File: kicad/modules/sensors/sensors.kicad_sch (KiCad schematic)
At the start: 44 parts, among them J1 Bus_PCI_Express_x1, J2 TYPE-C-31-M-04, J3 Conn_01x02, U2 RP2040, U4 W25Q128JVP, U5 BMP388, U8 BNO055, U9 MCP25625T-E/ML, X1 ABM8-272-T3, Y1 ABS07-32.768KHZ-T, Y2 X322516MLB4SI

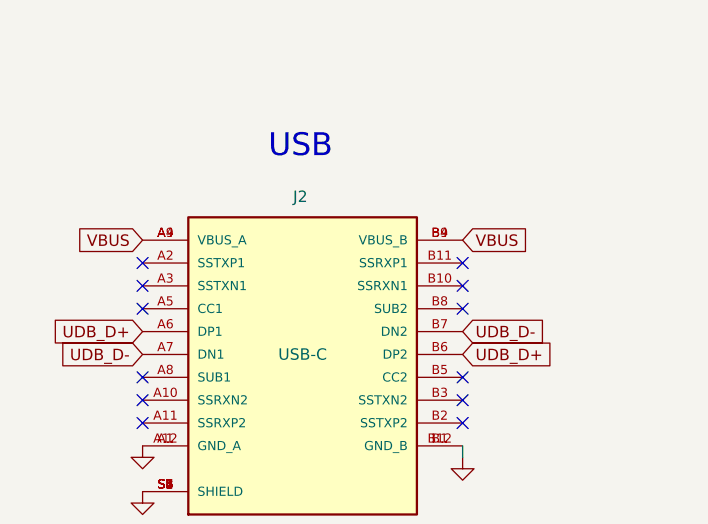
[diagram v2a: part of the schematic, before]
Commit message: add no connect to USB power pins
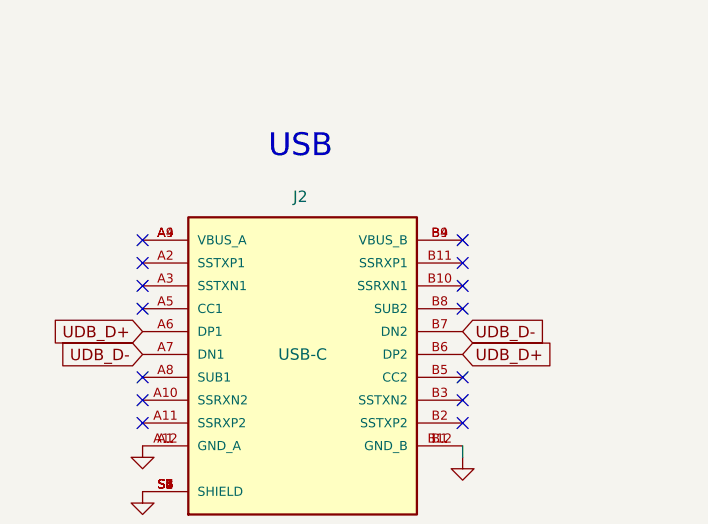
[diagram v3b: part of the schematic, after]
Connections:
- net VBUS: no longer names the net of J2.A4 (VBUS_A), J2.A9 (VBUS_A)
- net VBUS: no longer J2.B4 (VBUS_B), J2.B9 (VBUS_B)
- new net: J2.B4 (VBUS_B), J2.B9 (VBUS_B)
- no-connect marks 18 -> 20
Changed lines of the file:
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@@
+	)
+	(no_connect
+		(at 93.98 62.23)
+	)
+	(no_connect
+		(at 58.42 67.31)
+	)
+	(no_connect
+		(at 58.42 80.01)
+	)
+	(no_connect
+		(at 346.71 342.9)
+	)
+	(no_connect
+		(at 346.71 345.44)
 	)
 	(no_connect
@@
 	)
 	(no_connect
-		(at 58.42 67.31)
-	)
-	(no_connect
-		(at 58.42 80.01)
-	)
-	(no_connect
-		(at 346.71 342.9)
-	)
-	(no_connect
-		(at 346.71 345.44)
-	)
-	(no_connect
 		(at 93.98 77.47)
 	)
@@
 	(no_connect
 		(at 93.98 82.55)
+	)
+	(no_connect
+		(at 58.42 62.23)
 	)
 	(no_connect
@@
 		)
 	)
-	(global_label "VBUS"
-		(shape input)
-		(at 58.42 62.23 180)
+	(global_label "SI"
+		(shape input)
+		(at 378.46 220.98 0)
+		(fields_autoplaced yes)
+		(effects
+			(font
+				(size 1.27 1.27)
+			)
+			(justify left)
+		)
+		(property "Intersheetrefs" "${INTERSHEET_REFS}"
+			(at 383.2595 220.98 0)
+			(effects
+				(font
+					(size 1.27 1.27)
+				)
+				(justify left)
+				(hide yes)
+			)
+		)
+	)
+	(global_label "SO"
+		(shape input)
+		(at 378.46 223.52 0)
+		(fields_autoplaced yes)
+		(effects
+			(font
+				(size 1.27 1.27)
+			)
+			(justify left)
+		)
+		(property "Intersheetrefs" "${INTERSHEET_REFS}"
+			(at 383.9852 223.52 0)
+			(effects
+				(font
+					(size 1.27 1.27)
+				)
+				(justify left)
+				(hide yes)
+			)
+		)
+	)
+	(global_label "BMPINT"
+		(shape input)
+		(at 378.46 200.66 0)
+		(fields_autoplaced yes)
+		(effects
+			(font
+				(size 1.27 1.27)
+			)
+			(justify left)
+		)
+		(property "Intersheetrefs" "${INTERSHEET_REFS}"
+			(at 388.3395 200.66 0)
+			(effects
+				(font
+					(size 1.27 1.27)
+				)
+				(justify left)
+				(hide yes)
+			)
+		)
+	)
+	(global_label "tx"
+		(shape input)
+		(at 397.51 363.22 0)
+		(fields_autoplaced yes)
+		(effects
+			(font
+				(size 1.27 1.27)
+			)
+			(justify left)
+		)
+		(property "Intersheetrefs" "${INTERSHEET_REFS}"
+			(at 402.249 363.22 0)
+			(effects
+				(font
+					(size 1.27 1.27)
+				)
+				(justify left)
+				(hide yes)
+			)
+		)
+	)
+	(global_label "CS"
+		(shape input)
+		(at 346.71 330.2 180)
 		(fields_autoplaced yes)
 		(effects
@@
 		)
 		(property "Intersheetrefs" "${INTERSHEET_REFS}"
-			(at 50.5362 62.23 0)
+			(at 341.2453 330.2 0)
 			(effects
 				(font
@@
 		)
 	)
+	(global_label "BOOT_LOAD"
+		(shape input)
+		(at 471.17 278.13 180)
+		(fields_autoplaced yes)
+		(effects
+			(font
+				(size 1.27 1.27)
+			)
+			(justify right)
+		)
+		(property "Intersheetrefs" "${INTERSHEET_REFS}"
+			(at 457.6014 278.13 0)
+			(effects
+				(font
+					(size 1.27 1.27)
+				)
+				(justify right)
+				(hide yes)
+			)
+		)
+	)
 	(global_label "SI"
 		(shape input)
-		(at 378.46 220.98 0)
+		(at 397.51 335.28 0)
 		(fields_autoplaced yes)
 		(effects
@@
 		)
 		(property "Intersheetrefs" "${INTERSHEET_REFS}"
-			(at 383.2595 220.98 0)
+			(at 402.3095 335.28 0)
 			(effects
 				(font
@@
 		)
 	)
-	(global_label "SO"
-		(shape input)
-		(at 378.46 223.52 0)
+	(global_label "SCL"
+		(shape input)
+		(at 491.49 288.29 180)
+		(fields_autoplaced yes)
+		(effects
+			(font
+				(size 1.27 1.27)
+			)
+			(justify right)
+		)
+		(property "Intersheetrefs" "${INTERSHEET_REFS}"
+			(at 484.9972 288.29 0)
+			(effects
+				(font
+					(size 1.27 1.27)
+				)
+				(justify right)
+				(hide yes)
+			)
+		)
+	)
+	(global_label "CANSTBY"
+		(shape input)
+		(at 378.46 233.68 0)
 		(fields_autoplaced yes)
 		(effects
@@
 		)
 		(property "Intersheetrefs" "${INTERSHEET_REFS}"
-			(at 383.9852 223.52 0)
+			(at 389.67 233.68 0)
 			(effects
 				(font
@@
 		)
 	)
-	(global_label "BMPINT"
-		(shape input)
-		(at 378.46 200.66 0)
+	(global_label "OSC2"
+		(shape input)
+		(at 397.51 353.06 0)
 		(fields_autoplaced yes)
 		(effects
@@
 		)
 		(property "Intersheetrefs" "${INTERSHEET_REFS}"
-			(at 388.3395 200.66 0)
-			(effects
-				(font
-					(size 1.27 1.27)
-				)
-				(justify left)
-				(hide yes)
-			)
-		)
-	)
-	(global_label "tx"
-		(shape input)
-		(at 397.51 363.22 0)
-		(fields_autoplaced yes)
-		(effects
-			(font
-				(size 1.27 1.27)
-			)
-			(justify left)
-		)
-		(property "Intersheetrefs" "${INTERSHEET_REFS}"
-			(at 402.249 363.22 0)
-			(effects
-				(font
-					(size 1.27 1.27)
-				)
-				(justify left)
-				(hide yes)
-			)
-		)
-	)
-	(global_label "CS"
-		(shape input)
-		(at 346.71 330.2 180)
-		(fields_autoplaced yes)
-		(effects
-			(font
-				(size 1.27 1.27)
-			)
-			(justify right)
-		)
-		(property "Intersheetrefs" "${INTERSHEET_REFS}"
-			(at 341.2453 330.2 0)
-			(effects
-				(font
-					(size 1.27 1.27)
-				)
-				(justify right)
-				(hide yes)
-			)
-		)
-	)
-	(global_label "BOOT_LOAD"
-		(shape input)
-		(at 471.17 278.13 180)
-		(fields_autoplaced yes)
-		(effects
-			(font
-				(size 1.27 1.27)
-			)
-			(justify right)
-		)
-		(property "Intersheetrefs" "${INTERSHEET_REFS}"
-			(at 457.6014 278.13 0)
-			(effects
-				(font
-					(size 1.27 1.27)
-				)
-				(justify right)
-				(hide yes)
-			)
-		)
-	)
-	(global_label "SI"
-		(shape input)
-		(at 397.51 335.28 0)
-		(fields_autoplaced yes)
-		(effects
-			(font
-				(size 1.27 1.27)
-			)
-			(justify left)
-		)
-		(property "Intersheetrefs" "${INTERSHEET_REFS}"
-			(at 402.3095 335.28 0)
-			(effects
-				(font
-					(size 1.27 1.27)
-				)
-				(justify left)
-				(hide yes)
-			)
-		)
-	)
-	(global_label "SCL"
-		(shape input)
-		(at 491.49 288.29 180)
-		(fields_autoplaced yes)
-		(effects
-			(font
-				(size 1.27 1.27)
-			)
-			(justify right)
-		)
-		(property "Intersheetrefs" "${INTERSHEET_REFS}"
-			(at 484.9972 288.29 0)
-			(effects
-				(font
-					(size 1.27 1.27)
-				)
-				(justify right)
-				(hide yes)
-			)
-		)
-	)
-	(global_label "CANSTBY"
-		(shape input)
-		(at 378.46 233.68 0)
-		(fields_autoplaced yes)
-		(effects
-			(font
-				(size 1.27 1.27)
-			)
-			(justify left)
-		)
-		(property "Intersheetrefs" "${INTERSHEET_REFS}"
-			(at 389.67 233.68 0)
-			(effects
-				(font
-					(size 1.27 1.27)
-				)
-				(justify left)
-				(hide yes)
-			)
-		)
-	)
-	(global_label "OSC2"
-		(shape input)
-		(at 397.51 353.06 0)
-		(fields_autoplaced yes)
-		(effects
-			(font
-				(size 1.27 1.27)
-			)
-			(justify left)
-		)
-		(property "Intersheetrefs" "${INTERSHEET_REFS}"
 			(at 405.5147 353.06 0)
 			(effects
 				(font
-					(size 1.27 1.27)
-				)
-				(justify left)
-				(hide yes)
-			)
-		)
-	)
-	(global_label "VBUS"
-		(shape input)
-		(at 93.98 62.23 0)
-		(fields_autoplaced yes)
-		(effects
-			(font
-				(size 1.27 1.27)
-			)
-			(justify left)
-		)
-		(property "Intersheetrefs" "${INTERSHEET_REFS}"
-			(at 101.8638 62.23 0)
-			(effects
-				(font

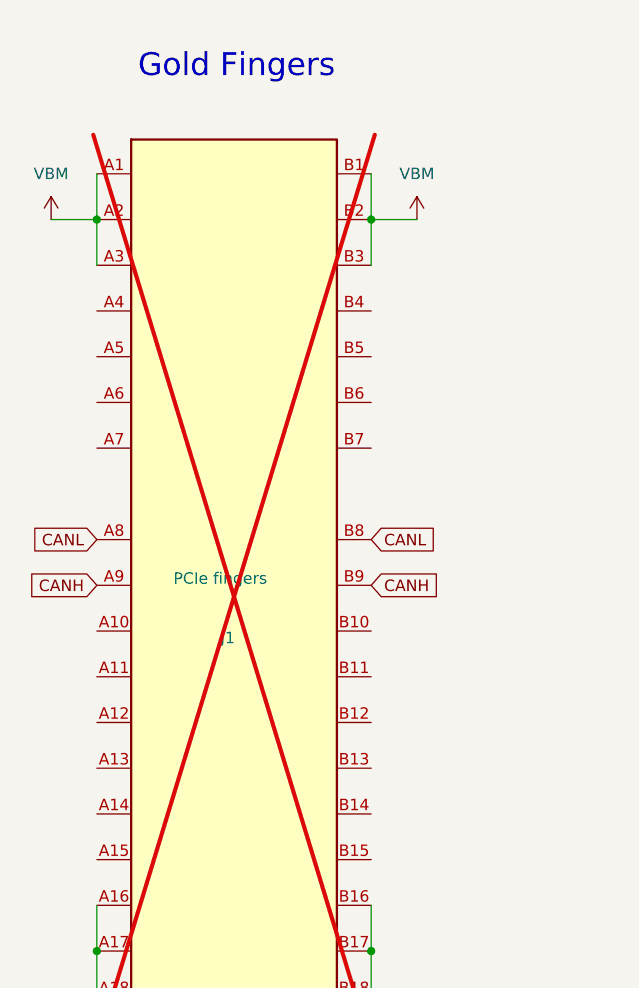
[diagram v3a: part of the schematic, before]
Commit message: reassign PCIe pins
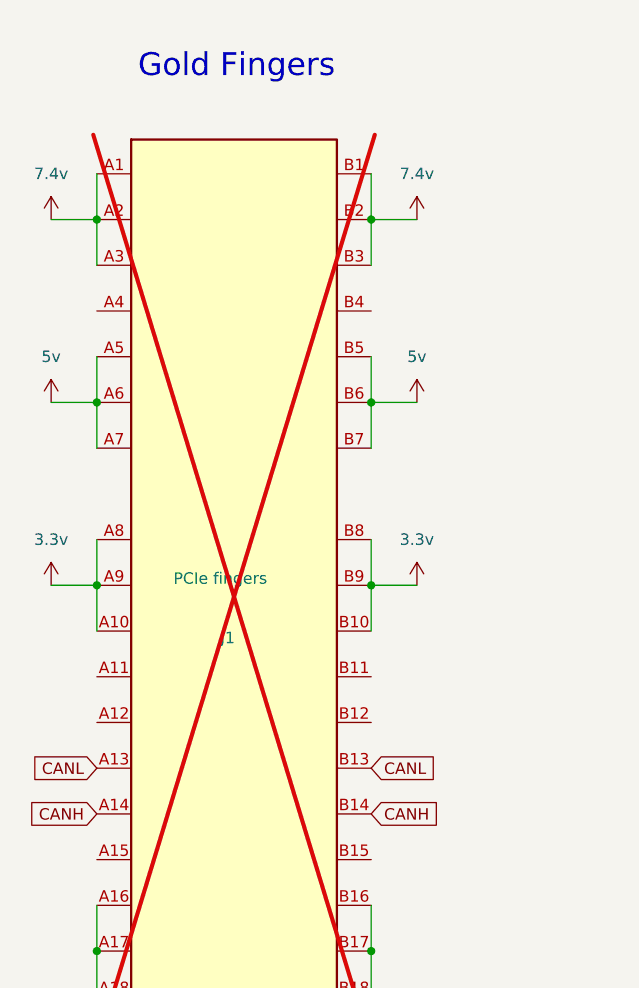
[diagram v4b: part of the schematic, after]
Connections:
- net CANH: now also J1.A14 (REFCLK-), J1.B14 (PETp0); no longer J1.A9 (+3.3V), J1.B9 (JTAG1)
- net CANL: now also J1.A13 (REFCLK+), J1.B13 (GND); no longer J1.A8 (JTAG5), J1.B8 (+3.3V)
- net 3.3v: now reaches J1.A10 (+3.3V)
- net 3.3v: now also J1.A8 (JTAG5), J1.A9 (+3.3V), J1.B10 (3.3Vaux), J1.B8 (+3.3V), J1.B9 (JTAG1)
- net 5v: now reaches J1.A5 (JTAG2)
- net 5v: now also J1.A6 (JTAG3), J1.A7 (JTAG4), J1.B5 (SMCLK), J1.B6 (SMDAT), J1.B7 (GND)
- net VBM renamed 7.4v

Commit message: fix voltage labels
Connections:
- net 3.3v is gone; now on net +3.3V: J1.A10 (+3.3V), J1.A8 (JTAG5), J1.A9 (+3.3V), J1.B10 (3.3Vaux), J1.B8 (+3.3V), J1.B9 (JTAG1)
- net 5v is gone; now on net +5V: J1.A5 (JTAG2), J1.A6 (JTAG3), J1.A7 (JTAG4), J1.B5 (SMCLK), J1.B6 (SMDAT), J1.B7 (GND)
- net +3.3V: now also C200.1, C201.1, C202.1, C203.1, C204.1, C205.1, C206.1, C210.1, C40.1, C81.1, C82.2, R83.2, R87.2, U2.1 (IOVDD), U2.10 (IOVDD), U2.22 (IOVDD), U2.33 (IOVDD), U2.42 (IOVDD), U2.43 (ADC_AVDD), U2.44 (VREG_IN), U2.48 (USB_VDD), U2.49 (IOVDD), U4.8 (VCC), U8.28 (VDDIO), U8.3 (VDD)
- net +3V3: no longer C200.1, C201.1, C202.1, C203.1, C204.1, C205.1, C206.1, C210.1, C40.1, C81.1, C82.2, R83.2, R87.2, U2.1 (IOVDD), U2.10 (IOVDD), U2.22 (IOVDD), U2.33 (IOVDD), U2.42 (IOVDD), U2.43 (ADC_AVDD), U2.44 (VREG_IN), U2.48 (USB_VDD), U2.49 (IOVDD), U4.8 (VCC), U8.28 (VDDIO), U8.3 (VDD)
- net +1V1 renamed +1.1V
- net 7.4v renamed +7.4V
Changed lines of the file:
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@@
 	(text "IMU"
 		(exclude_from_sim no)
-		(at 507.492 245.618 0)
+		(at 505.206 241.808 0)
 		(effects
 			(font
@@
 			)
 		)
-		(property "Value" "3.3v"
+		(property "Value" "+3.3V"
 			(at 48.26 292.1 0)
 			(effects
@@
 			)
 		)
-		(property "Value" "5v"
+		(property "Value" "+5V"
 			(at 88.9 271.78 0)
 			(effects
@@
 			)
 		)
-		(property "Value" "5v"
+		(property "Value" "+5V"
 			(at 48.26 271.78 0)
 			(effects
@@
 			)
 		)
-		(property "Value" "+3V3"
+		(property "Value" "+3.3V"
 			(at 136.271 137.8458 0)
 			(effects
@@
 			)
 		)
-		(property "Value" "3.3v"
+		(property "Value" "+3.3V"
 			(at 88.9 292.1 0)
 			(effects
@@
 			)
 		)
-		(property "Value" "7.4v"
+		(property "Value" "+7.4V"
 			(at 88.9 251.46 0)
 			(effects
@@
 			)
 		)
-		(property "Value" "+3V3"
+		(property "Value" "+3.3V"
 			(at 485.902 249.682 0)
 			(effects
@@
 			)
 		)
-		(property "Value" "+3V3"
+		(property "Value" "+3.3V"
 			(at 474.472 249.682 0)
 			(effects
@@
 			)
 		)
-		(property "Value" "+1V1"
+		(property "Value" "+1.1V"
 			(at 339.471 144.1958 0)
 			(effects
@@
 			)
 		)
-		(property "Value" "+3V3"
+		(property "Value" "+3.3V"
 			(at 361.061 146.7358 0)
 			(effects
@@
 			)
 		)
-		(property "Value" "+3V3"
+		(property "Value" "+3.3V"
 			(at 509.016 247.396 0)
 			(effects
@@
 			)
 		)
-		(property "Value" "7.4v"
+		(property "Value" "+7.4V"
 			(at 48.26 251.46 0)
 			(effects

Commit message: add momentary buttons to schematic
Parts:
- removed J3: Conn_01x02, Connector_PinHeader_2.54mm:PinHeader_1x02_P2.54mm_Vertical, symbol Connector_Generic:Conn_01x02
- added J4: Conn_01x02, Connector_PinHeader_2.54mm:PinHeader_1x02_P2.54mm_Vertical, symbol Connector_Generic:Conn_01x02
- added S1, S2: TS-1187A-B-A-B, TS-1187A-B-A-B:SW_TS-1187A-B-A-B, symbol TS-1187A-B-A-B:TS-1187A-B-A-B
- renumbered C208 to C206, C209 to C208, C206 to C209, C205 to C211, C204 to C212, C203 to C213, C202 to C214, C201 to C215, C200 to C216, R213 to R203, R214 to R204, R211 to R220, R212 to R221
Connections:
- net GND: now also U2.19 (TESTEN), S1.A, S1.B, S2.A, S2.B
- net QSPI_SD0: now also U2.53 (QSPI_SD0)
- net QSPI_SD1: now also U2.55 (QSPI_SD1)
- net QSPI_SD2: now also U2.54 (QSPI_SD2)
- net QSPI_SD3: now also U2.51 (QSPI_SD3)
- net ~{USB_BOOT_S}: now also S1.C, S1.D
- net SWCLK: now reaches U2.24 (SWCLK)
- net SWCLK: now also J4.1 (Pin_1)
- net SWD: now reaches U2.25 (SWD)
- net SWD: now also J4.2 (Pin_2)
- net RUN: now reaches U2.26 (RUN)
- net RUN: now also S2.C, S2.D
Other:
- moved on the sheet: R30

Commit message: begin routing
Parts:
- X1: footprint crystal:ABM8-272-T3_ABR -> ABM8-272-T3:ABM8-272-T3_ABR
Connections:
- net XOUT_pre: now reaches C11.1, R12.2, X1.3
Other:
- moved on the sheet: C10, C11, C206, C207, C208, C209, C210, C211, C212, C213, C214, C215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

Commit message: finish most routing
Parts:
- added R222, R223: 4.7k, Resistor_SMD:R_0402_1005Metric, symbol Device:R
- S1, S2: JLC Link (none) -> https://jlcpcb.com/partdetail/XKBConnection-TS_1187A_B_AB/C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; LCSC Part # (none) -> C318884; basic? (none) -> yes; info (none) -> Button; price (none) -> C$0.0242
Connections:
- net +3V3 is gone; now on net +3.3V: R220.1, R221.2
- net UDB_D+ is gone; now on net USB_D+: J2.A6 (DP1), J2.B6 (DP2)
- net UDB_D- is gone; now on net USB_D-: J2.A7 (DN1), J2.B7 (DN2)
- net +3.3V: now also R222.2, R223.1
- net BMPINT: now also U2.39 (GPIO27_ADC1); no longer U2.5 (GPIO3)
- net CANH: now also J1.A13 (REFCLK+), J1.B13 (GND); no longer J1.A14 (REFCLK-), J1.B14 (PETp0)
- net CANINT: now also U2.32 (GPIO21); no longer U2.28 (GPIO17)
- net CANL: now also J1.A14 (REFCLK-), J1.B14 (PETp0); no longer J1.A13 (REFCLK+), J1.B13 (GND)
- net CANRESET: now also U2.27 (GPIO16)
- net CANSTBY: now also U2.38 (GPIO26_ADC0); no longer U2.27 (GPIO16)
- net CS: now also U2.28 (GPIO17); no longer U2.16 (GPIO13)
- net SCK: now also U2.31 (GPIO20); no longer U2.17 (GPIO14)
- net SI: now also U2.30 (GPIO19); no longer U2.14 (GPIO11)
- net SO: now also U2.29 (GPIO18); no longer U2.15 (GPIO12)
- net SDA1: now reaches U2.4 (GPIO2)
- net SDA1: now also R220.2, U8.20 (COM0)
- net SDA0: now reaches U2.40 (GPIO28_ADC2)
- net SDA0: now also U5.4 (SDI), R223.2
- net SCL0: now reaches U2.41 (GPIO29_ADC3)
- net SCL0: now also U5.2 (SCK), R222.1
- net SCL renamed SCL1
- net SCL1: now also U2.5 (GPIO3); no longer U2.3 (GPIO1), U5.2 (SCK)
- removed net SDA: R220.2, U2.2 (GPIO0), U5.4 (SDI), U8.20 (COM0)
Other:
- moved on the sheet: R220, R221
